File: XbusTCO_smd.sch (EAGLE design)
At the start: 111 parts, among them IC1 74HC4515D, IC2 PIC16F628P, IC3 MAX481CSA, IC4 78L05SMD, X1 1751264

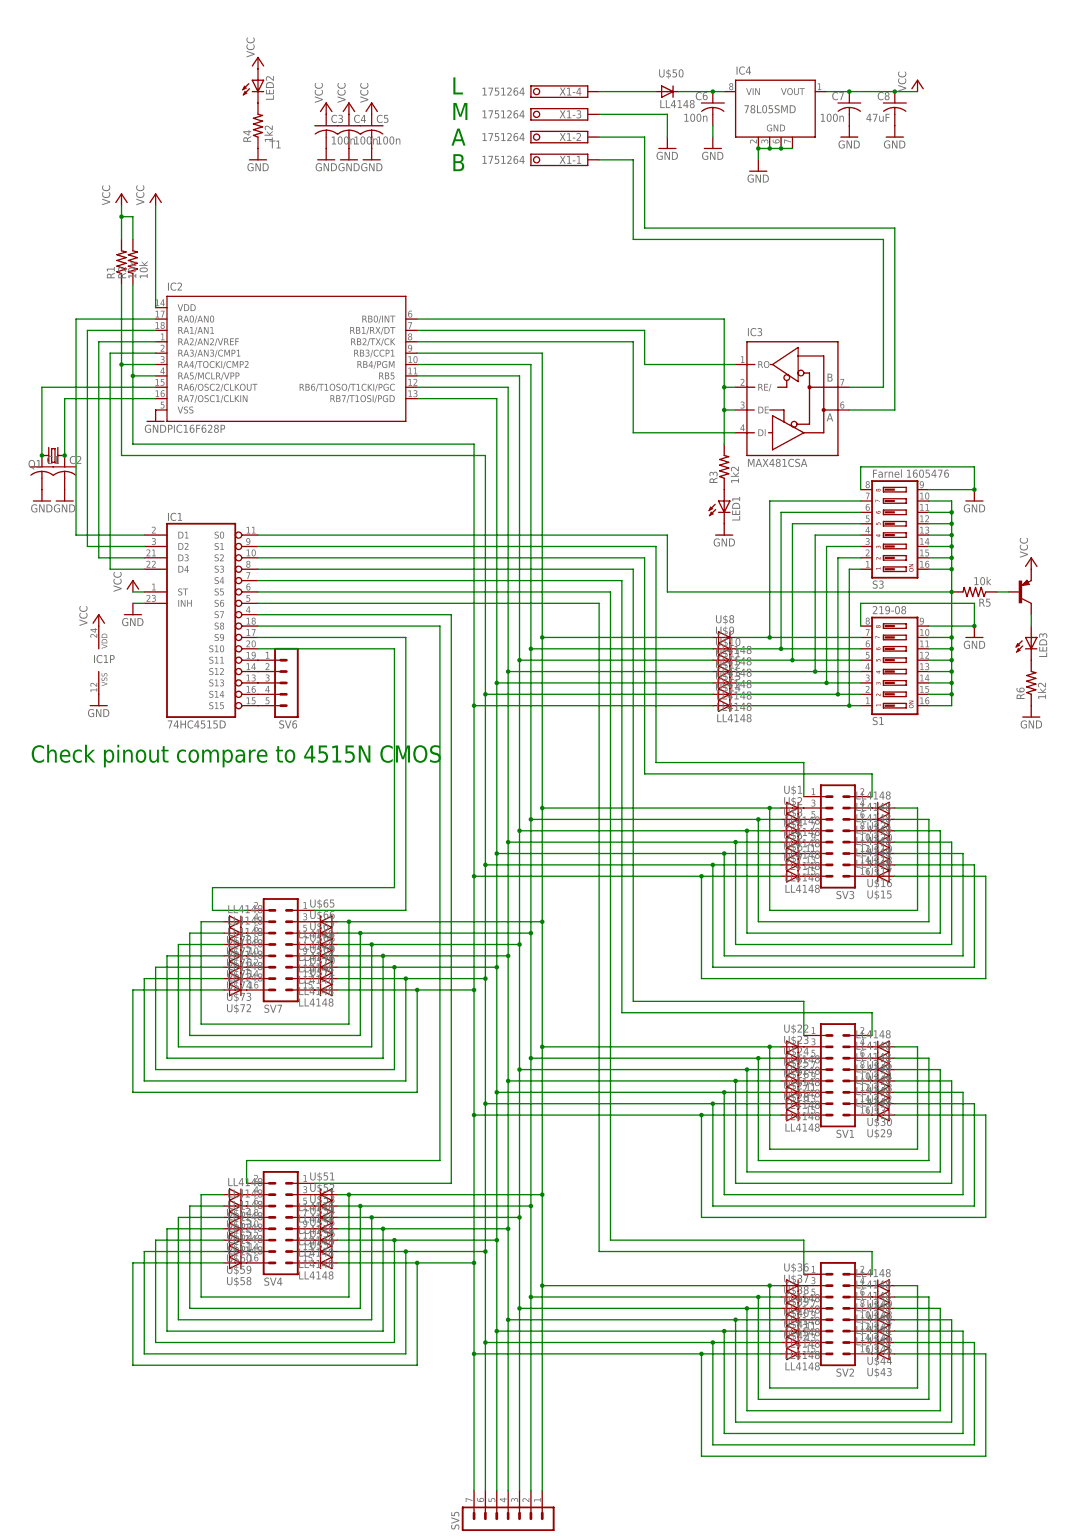
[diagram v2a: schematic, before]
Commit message: Added pdf files, added smd component size in value field.
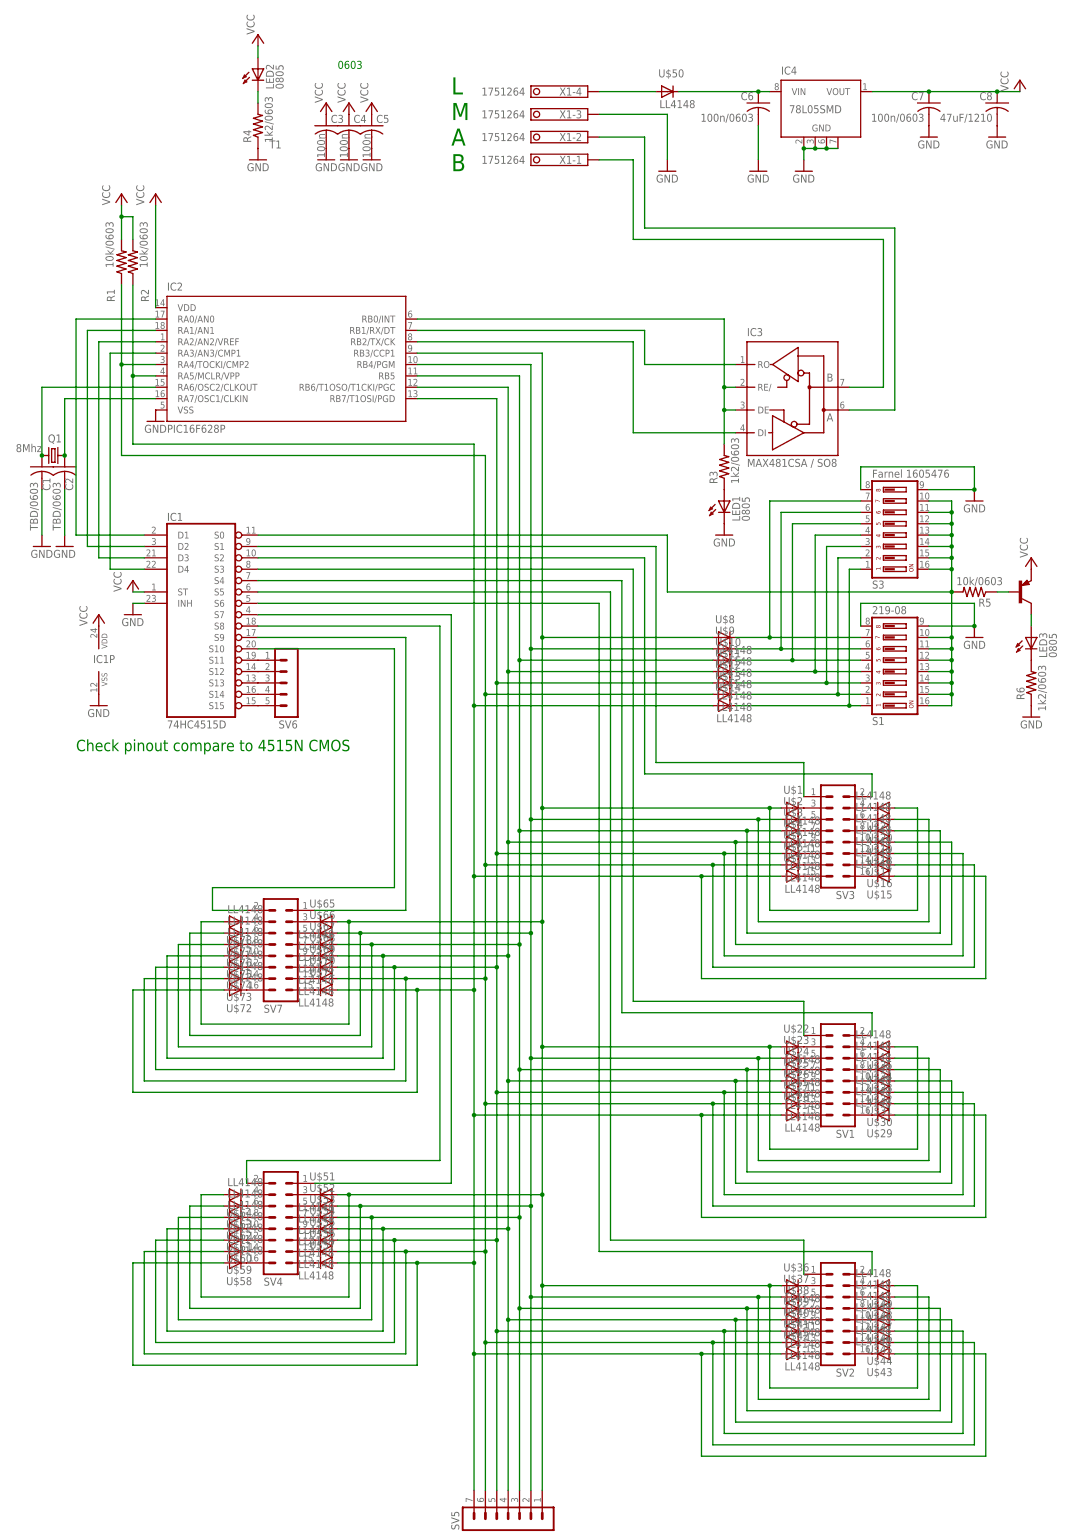
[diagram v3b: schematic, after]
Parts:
- C1, C2: value (none) -> TBD/0603
- C6, C7: value 100n -> 100n/0603
- C8: value 47uF -> 47uF/1210
- IC3: value MAX481CSA -> MAX481CSA / SO8
- LED1, LED2, LED3: value (none) -> 0805
- Q1: value (none) -> 8Mhz
- R1, R2, R5: value 10k -> 10k/0603
- R3, R4, R6: value 1k2 -> 1k2/0603
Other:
- note added: "0603"
- moved on the sheet: C6, C7, C8, IC4, LED2
